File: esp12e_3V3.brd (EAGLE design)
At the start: 50 x 50 mm, 26 parts, among them IC1 117\33

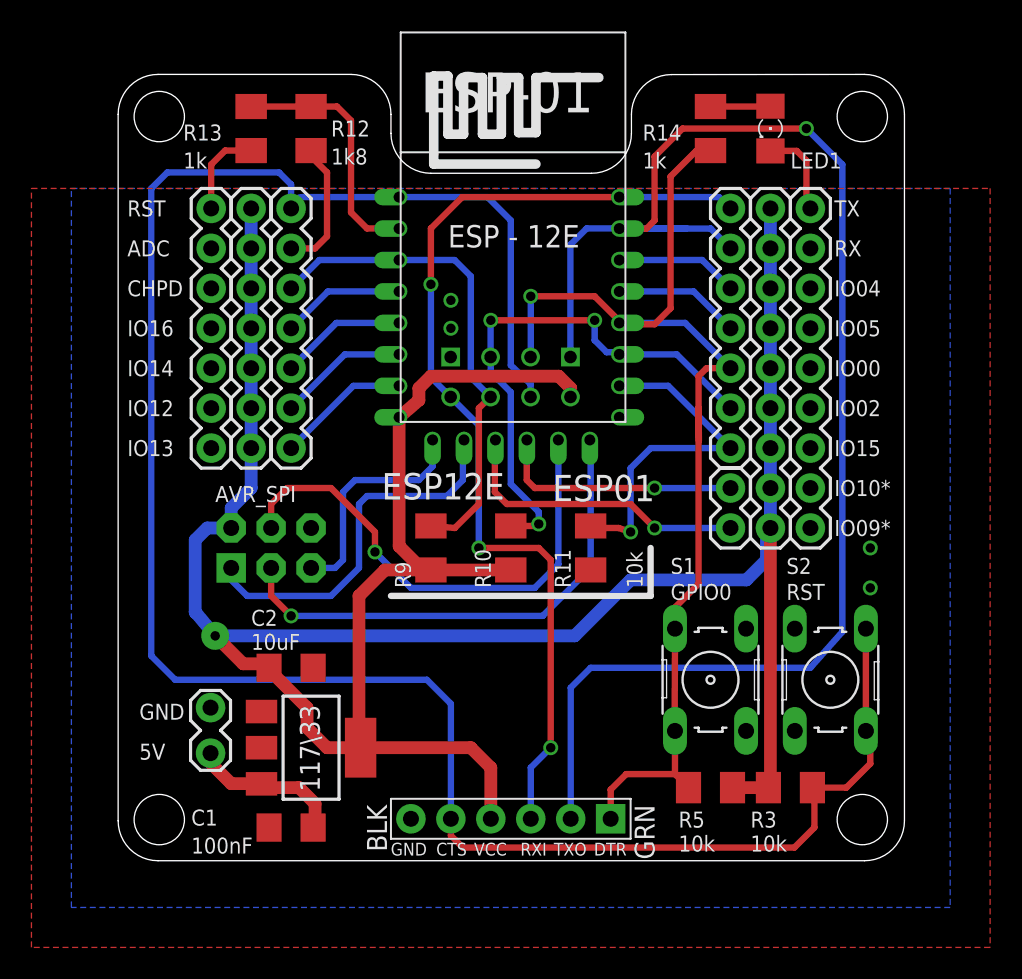
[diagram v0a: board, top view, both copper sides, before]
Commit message: esp12e revision
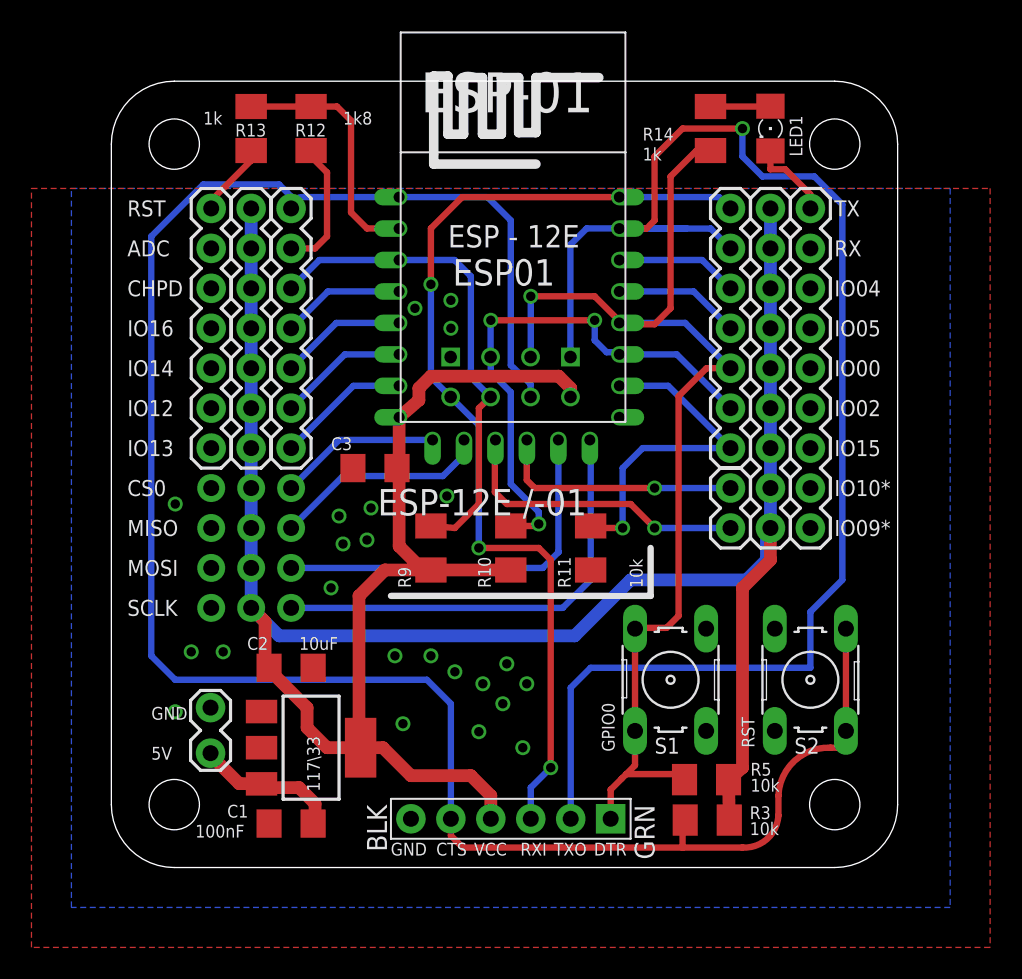
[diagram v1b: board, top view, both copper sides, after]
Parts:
- removed JP6: AVR_SPI, SparkFun-Connectors:2X3-NS
- added C3: 100nF, resistor:C1206
- added CN1, CN2, CN3: 1X4-CLEANBIG, adafruit:1X04-CLEANBIG
- added PCB1: PCB_DP_SQUARE-5X5, dp_pcb:DP5050_V1
- U$3: value ESP12E -> ESP-12E /-01
- moved R3 5.68 mm to (37.9, 3.02), turned to 180 degrees
- moved S1 2.54 mm to (35.6, 11.9)
- moved S2 1.27 mm to (44.5, 11.9)
- moved R5 0.57 mm to (37.8, 5.59)
- moved C1 0.25 mm to (11.4, 2.79)
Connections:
- removed net N$12: JP6.3, U$3.SCLK
- removed net N$13: JP6.5, U$3.CS0
- new net N$2: CN1.4, U$3.CS0
- new net N$6: CN1.3, U$3.MISO
- net +3V3: now also C3.2, CN2.1, CN2.2, CN2.3, CN2.4; no longer JP6.2
- net GND: now also C3.1, CN3.1, CN3.2, CN3.3, CN3.4; no longer JP6.6
- net N$10: now also CN1.2, U$3.MOSI; no longer JP6.1, U$3.MISO
- net N$11: now also CN1.1, U$3.SCLK; no longer JP6.4, U$3.MOSI
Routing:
- net N$12: track 32.0 -> 0.00 mm, vias 1 -> 0
- net N$13: track 14.6 -> 0.00 mm
- net N$6: track 0.00 -> 13.9 mm
- net N$2: track 0.00 -> 10.3 mm
- net +3V3: track 181.1 -> 175.0 mm, vias 1 -> 0
- net N$1: track 135.8 -> 131.4 mm
- net N$11: track 32.1 -> 28.7 mm, vias 1 -> 0
- net GPIO0: track 73.5 -> 71.8 mm
- net GND: track 12.9 -> 11.5 mm, vias 4 -> 23
- net N$10: track 23.9 -> 24.6 mm
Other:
- outline, holes or cut-outs redrawn
- board text added: "CS0"
- board text added: "MISO"
- board text added: "MOSI"
- board text added: "SCLK"
